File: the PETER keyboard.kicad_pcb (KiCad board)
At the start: 2 copper layers, 142 parts, among them SW1 RotaryEncoder_Switch, SW12 RotaryEncoder_Switch, SW2 SW_Push, U1 ATmega32U4-A, Y1 Crystal_GND24_Small

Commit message: Switches and Diodes placed, margins assigned
still need to figure out placement of usb, and MCU
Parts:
- D1, D10, D11, D12, D13, D14, D15, D16, D17, D18, D19, D2, D20, D21, D22, D23, D24, D25, D26, D27, D28, D29, D3, D30, D31, D32, D33, D34, D35, D36, D37, D38, D39, D4, D40, D41, D42, D43, D44, D45, D46, D47, D48, D49, D5, D50, D51, D52, D53, D54, D55, D56, D57, D58, D6, D7, D8, D9, D_SW1, D_SW12, U1: moved to B.Cu
- moved D_SW12 243.8 mm to (243.7, 51.9), turned to 90 degrees
- moved D22 194.1 mm to (214.5, 80.4), turned to 90 degrees
- moved D12 182.7 mm to (243.7, 61.4), turned to 90 degrees
- moved D11 180.9 mm to (238.3, 61.4), turned to 90 degrees
- moved D36 172.7 mm to (259.7, 99.4), turned to 90 degrees
- moved D57 151.7 mm to (243.1, 137.5), turned to 90 degrees
- moved D8 150.5 mm to (181.1, 61.4), turned to 90 degrees
- moved D24 148.4 mm to (257.3, 80.4), turned to 90 degrees
- moved D7 143.0 mm to (162.1, 61.3), turned to 90 degrees
- moved D9 142.8 mm to (200.2, 61.4), turned to 90 degrees
- moved D10 142.8 mm to (219.2, 61.3), turned to 90 degrees
- moved D48 142.0 mm to (262.1, 118.5), turned to 90 degrees
- moved D35 141.5 mm to (238.3, 99.4), turned to 90 degrees
- moved D_SW1 140.7 mm to (44.6, 51.9), turned to 90 degrees
- moved D4 138.9 mm to (104.9, 61.3), turned to 90 degrees
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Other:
- board outline added: 245.5 x 102.5 mm

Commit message: matrix tracing
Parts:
- C_Decoupler1, C_Decoupler2, C_Decoupler3, C_Decoupler4, C_UCAP1, C_USBSHIELD1, C_crystal1, C_crystal2, D59, F_USBC1, R_HWB/PE2, R_USB1, R_USB2, R_USB3, R_USB4, R_USBSHIELD1, R_reset1, SW2, USB1, Y1: moved to B.Cu
- moved C_USBSHIELD1 168.7 mm to (155.1, 63.3), turned to 180 degrees
- moved H_USBSHIELD1 168.7 mm to (163.8, 47.6)
- moved R_USB2 129.7 mm to (146.9, 58.3), turned to 90 degrees
- moved R_USB1 126.2 mm to (139.0, 64.1), turned to -90 degrees
- moved R_USBSHIELD1 122.1 mm to (132.7, 62.7), turned to -90 degrees
- moved R_HWB/PE2 116.4 mm to (77.9, 105.2), turned to 90 degrees
- moved D59 110.5 mm to (147.7, 64.1), turned to 180 degrees
- moved C_crystal1 103.5 mm to (97.3, 105.5), turned to -90 degrees
- moved C_UCAP1 100.0 mm to (80.5, 124.6), turned to 180 degrees
- moved F_USBC1 97.4 mm to (106.4, 85.6), turned to 180 degrees
- moved R_USB4 96.4 mm to (114.6, 86.2), turned to 180 degrees
- moved C_Decoupler3 96.0 mm to (103.4, 121.5), turned to 90 degrees
- moved C_crystal2 89.9 mm to (90.0, 105.5), turned to 90 degrees
- moved C_Decoupler2 88.6 mm to (81.4, 105.1), turned to 90 degrees
- moved C_Decoupler1 80.2 mm to (94.8, 138.4), turned to 180 degrees
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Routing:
- net ROW4: track 0.00 -> 232.8 mm
- net ROW0: track 0.00 -> 223.9 mm
- net  ROW3: track 0.00 -> 218.7 mm
- net ROW2: track 0.00 -> 214.6 mm
- net ROW1: track 0.00 -> 214.3 mm
- net COL11: track 0.00 -> 91.0 mm
- net COL0: track 0.00 -> 90.0 mm
- net COL7: track 0.00 -> 87.0 mm
- net COL5: track 0.00 -> 86.0 mm
- net COL1: track 0.00 -> 84.1 mm
- net COL4: track 0.00 -> 83.1 mm
- net COL2: track 0.00 -> 83.1 mm
- net COL9: track 0.00 -> 82.1 mm
- net COL8: track 0.00 -> 82.1 mm
- net COL10: track 0.00 -> 82.1 mm
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
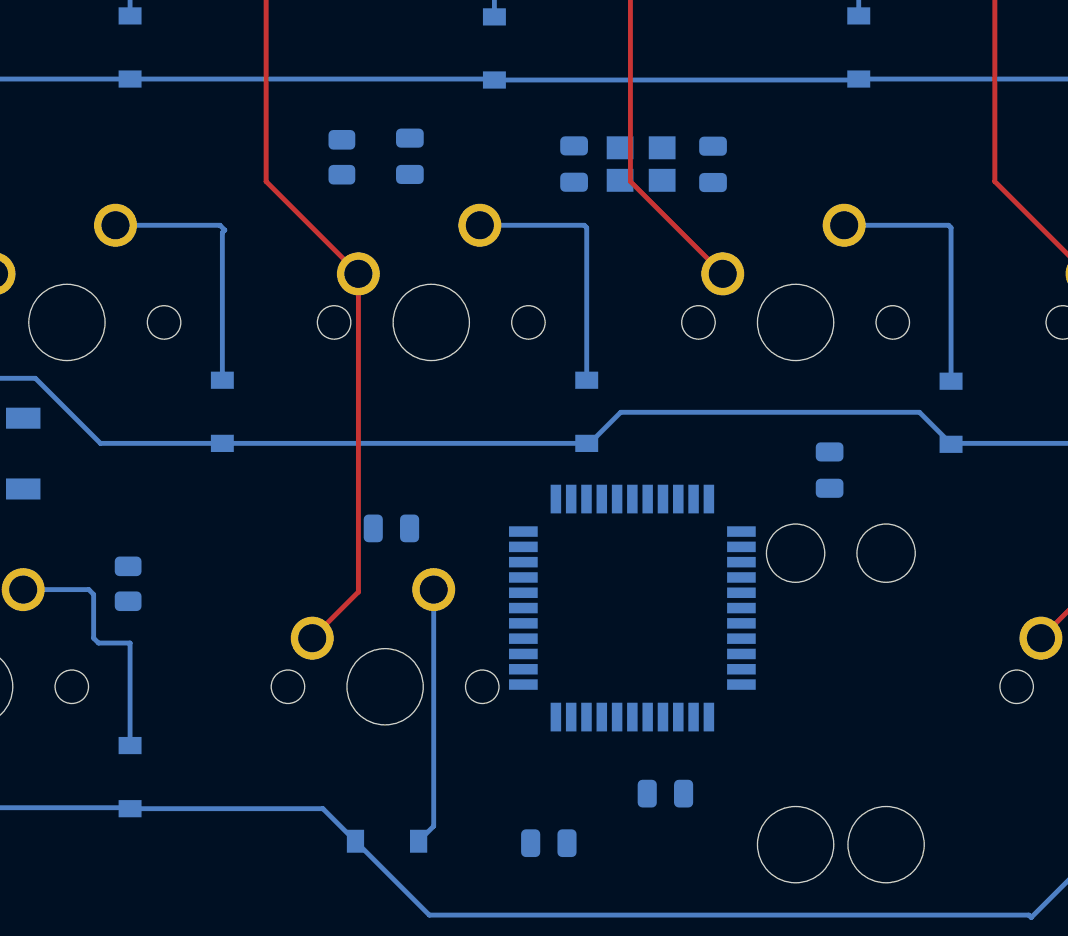
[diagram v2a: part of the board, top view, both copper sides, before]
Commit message: starting mcu traces
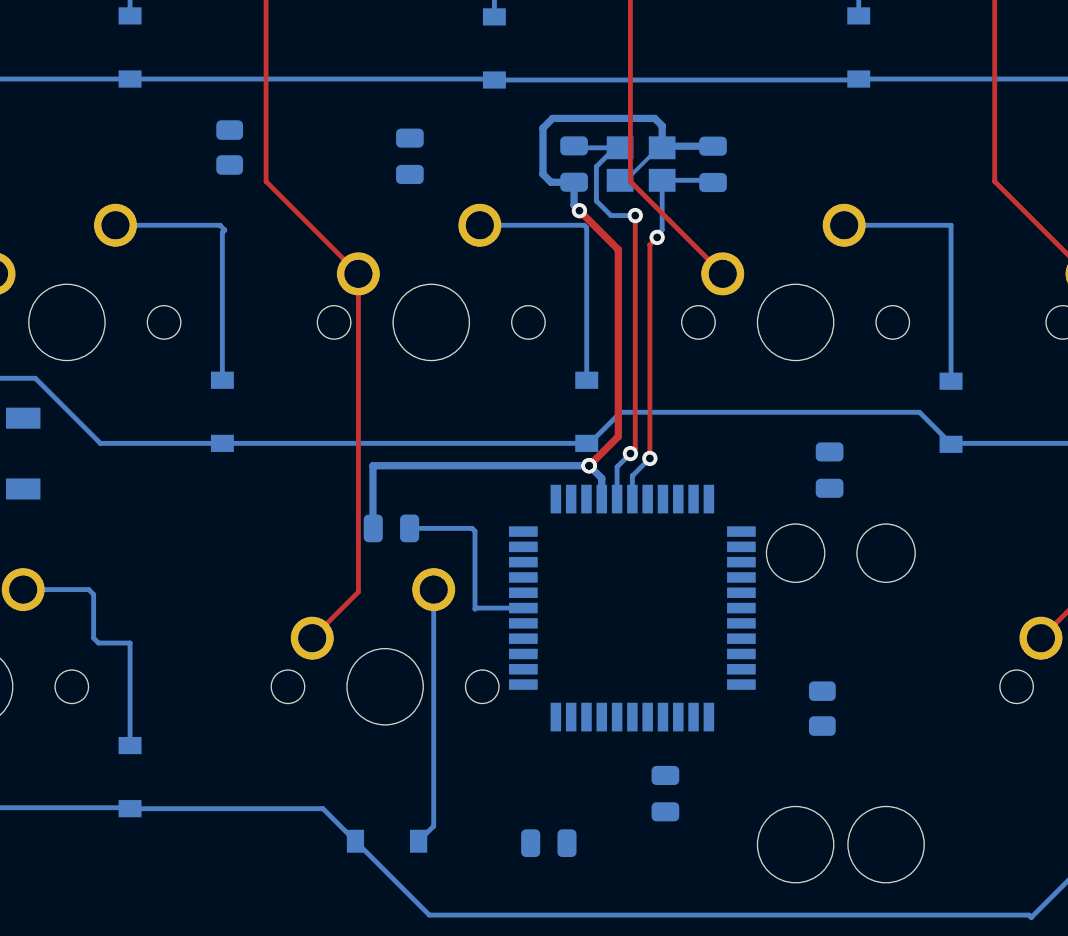
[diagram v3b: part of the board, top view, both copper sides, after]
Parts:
- moved R_HWB/PE2 38.2 mm to (103.0, 134.0), turned to -90 degrees
- moved R_reset1 23.4 mm to (72.0, 104.6)
- turned C_Decoupler1 to 90 degrees
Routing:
- net GND: track 0.00 -> 50.6 mm, vias 0 -> 3
- net Net-(C_crystal2-Pad2): track 0.00 -> 23.5 mm, vias 0 -> 2
- net Net-(C_crystal1-Pad2): track 0.00 -> 20.0 mm, vias 0 -> 2
- net Net-(C_UCAP1-Pad1): track 0.00 -> 10.1 mm

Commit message: reworked DSM placement, exchanged MCU for smaller
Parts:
- U1: value ATmega32U4-A -> ATmega32U4-M; footprint Package_QFP:TQFP-44_10x10mm_P0.8mm -> Package_DFN_QFN:QFN-44-1EP_7x7mm_P0.5mm_EP5.2x5.2mm
- moved R_USB3 83.6 mm to (94.0, 147.8)
- moved C_Decoupler2 46.6 mm to (70.1, 150.3)
- moved R_reset1 46.6 mm to (60.7, 149.9)
- moved C_UCAP1 39.8 mm to (72.8, 163.6)
- moved C_Decoupler3 36.8 mm to (83.3, 152.4)
- moved R_USB1 29.3 mm to (149.0, 36.4), turned to 180 degrees
- moved D59 26.9 mm to (143.8, 37.5)
- moved R_USB2 23.1 mm to (138.8, 36.6), turned to -90 degrees
- moved C_Decoupler1 20.7 mm to (101.6, 158.0)
- moved C_Decoupler4 18.8 mm to (95.2, 158.6)
- moved C_USBSHIELD1 18.7 mm to (153.2, 44.7), turned to -90 degrees
- moved R_USBSHIELD1 17.5 mm to (136.4, 45.6)
- moved C_crystal1 14.4 mm to (98.5, 119.9)
- moved C_crystal2 14.4 mm to (91.2, 119.9)
- moved Y1 14.4 mm to (94.7, 119.9)
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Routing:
- net ROW4: track 232.8 -> 0.00 mm
- net ROW0: track 223.9 -> 0.00 mm
- net  ROW3: track 218.7 -> 0.00 mm
- net ROW2: track 214.6 -> 0.00 mm
- net ROW1: track 214.3 -> 0.00 mm
- net GND: track 50.6 -> 0.00 mm, vias 3 -> 0
- net Net-(D_SW12-Pad2): track 32.5 -> 0.00 mm
- net Net-(C_crystal2-Pad2): track 23.5 -> 0.00 mm, vias 2 -> 0
- net Net-(D1-Pad2): track 21.9 -> 0.00 mm
- net Net-(D53-Pad2): track 21.0 -> 0.00 mm
- net Net-(C_crystal1-Pad2): track 20.0 -> 0.00 mm, vias 2 -> 0
- net Net-(D12-Pad2): track 17.2 -> 0.00 mm
- net Net-(D55-Pad2): track 14.0 -> 0.00 mm
- net Net-(D28-Pad2): track 13.9 -> 0.00 mm
- net Net-(D58-Pad2): track 13.9 -> 0.00 mm
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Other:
- board size 245.5 x 102.5 mm -> 241.6 x 96.9 mm

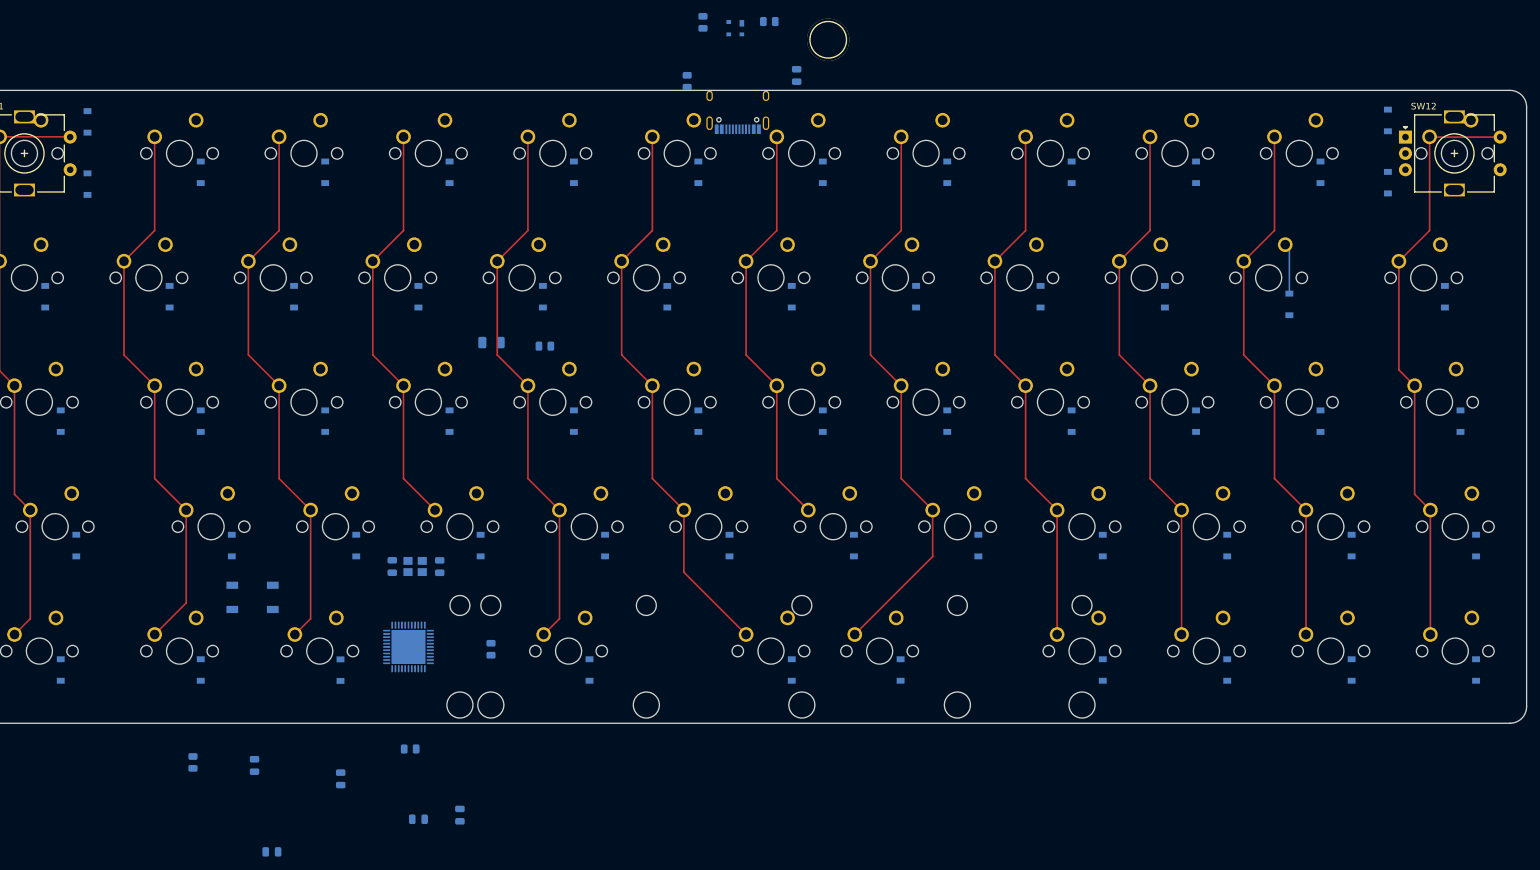
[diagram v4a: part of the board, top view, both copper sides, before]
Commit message: trying to trace mcu, usb
no success yet
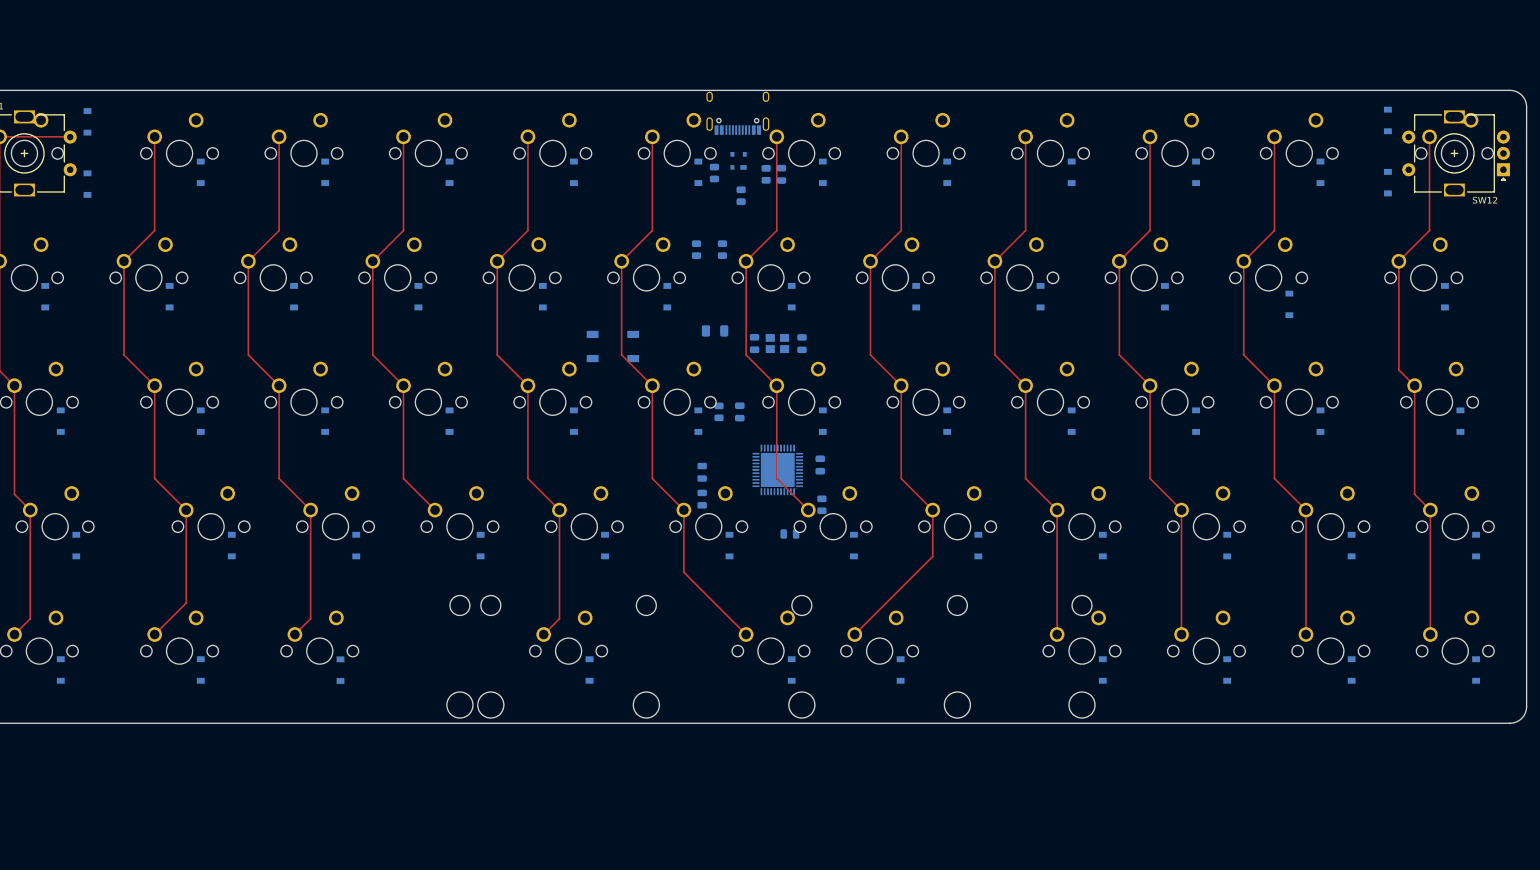
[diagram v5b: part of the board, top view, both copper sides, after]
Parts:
- removed H_USBSHIELD1: MountingHole_Pad, Keebio-Parts:MountingHole
- removed USB1: HRO-TYPE-C-31-M-12, Keebio-Parts:HRO-TYPE-C-31-M-12-Assembly
- added J1: USB_C_Receptacle_USB2.0, Connector_USB:USB_C_Receptacle_HRO_TYPE-C-31-M-12, B.Cu at (144.1, 49.0)
- R_USB1, R_USB2: value 5k1 -> 5.1k
- moved R_reset1 96.8 mm to (141.3, 96.2), turned to -90 degrees
- moved C_Decoupler2 89.3 mm to (152.1, 114.9), turned to 0 degrees
- moved R_USB3 88.1 mm to (137.8, 71.4), turned to -90 degrees
- moved C_UCAP1 87.8 mm to (138.7, 105.5), turned to -90 degrees
- moved C_Decoupler3 87.8 mm to (156.8, 104.3)
- moved C_Decoupler1 75.2 mm to (144.4, 96.2)
- moved SW2 67.2 mm to (125.0, 86.2)
- moved C_Decoupler4 65.5 mm to (138.7, 109.6), turned to -90 degrees
- moved C_crystal1 65.1 mm to (154.0, 85.8)
- moved C_crystal2 65.1 mm to (146.7, 85.8)
- moved Y1 65.1 mm to (150.2, 85.8)
- moved U1 62.7 mm to (150.3, 105.1)
- moved R_HWB/PE2 55.3 mm to (157.0, 110.4)
- moved F_USBC1 34.3 mm to (140.7, 83.8)
- moved R_USB4 30.9 mm to (141.8, 71.4), turned to -90 degrees
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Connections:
- net GNDREF renamed Net-(R_USBSHIELD1-Pad1)
- D59 pad 2: D+ -> D-
- R_USB3 pad 1: D+ -> D-
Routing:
- net COL11: track 91.0 -> 80.2 mm
- net Net-(D23-Pad2): track 7.76 -> 0.00 mm
- net Net-(D13-Pad2): track 1.29 -> 0.00 mm
- net Net-(D24-Pad2): track 1.11 -> 0.00 mm
- net Net-(D22-Pad2): track 1.09 -> 0.00 mm
- net Net-(D19-Pad2): track 1.09 -> 0.00 mm
- net Net-(D16-Pad2): track 1.09 -> 0.00 mm
- net Net-(D14-Pad2): track 1.09 -> 0.00 mm
- net Net-(D21-Pad2): track 1.09 -> 0.00 mm
- net Net-(D20-Pad2): track 1.09 -> 0.00 mm
- net Net-(D18-Pad2): track 1.09 -> 0.00 mm
- net Net-(D17-Pad2): track 1.09 -> 0.00 mm
- net Net-(D15-Pad2): track 0.90 -> 0.00 mm

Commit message: more attempts at changing mcu
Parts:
- moved U1 61.4 mm to (95.2, 132.2)
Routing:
- net  ROW3: track 0.00 -> 76.2 mm
- net ROW2: track 0.00 -> 57.2 mm
- net ROW4: track 0.00 -> 38.1 mm
- net GND: track 0.00 -> 17.1 mm
- net Net-(D23-Pad2): track 0.00 -> 7.76 mm
- net Net-(D49-Pad2): track 0.00 -> 6.62 mm
- net Net-(D25-Pad2): track 0.00 -> 6.62 mm
- net Net-(D51-Pad2): track 0.00 -> 6.61 mm
- net Net-(D6-Pad2): track 0.00 -> 6.61 mm
- net Net-(D11-Pad2): track 0.00 -> 6.61 mm
- net Net-(D35-Pad2): track 0.00 -> 6.61 mm
- net Net-(D30-Pad2): track 0.00 -> 6.61 mm
- net Net-(D50-Pad2): track 0.00 -> 6.61 mm
- net Net-(D4-Pad2): track 0.00 -> 6.61 mm
- net Net-(D3-Pad2): track 0.00 -> 6.61 mm
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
